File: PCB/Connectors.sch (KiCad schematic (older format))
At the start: 17 parts, among them J1 S2B-PH-SM4-TB, J10 DNP, J11 DNP, J12 DNP, J2 TRANSDUCER, J3 DNP, J4 PH1-08-UA, J5 DNP, J6 DNP, J7 DNP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

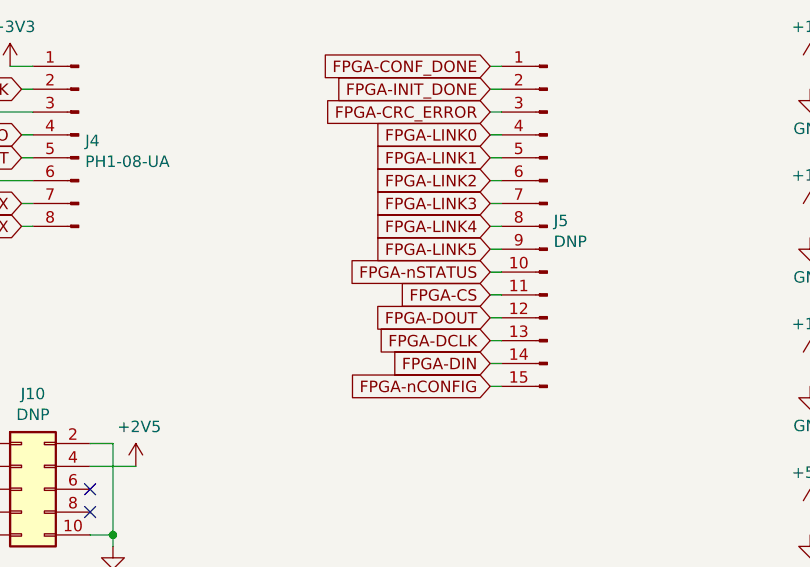
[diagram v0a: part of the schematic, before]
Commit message: Move FPGA SPI-DOUT pin to make Quartus happy
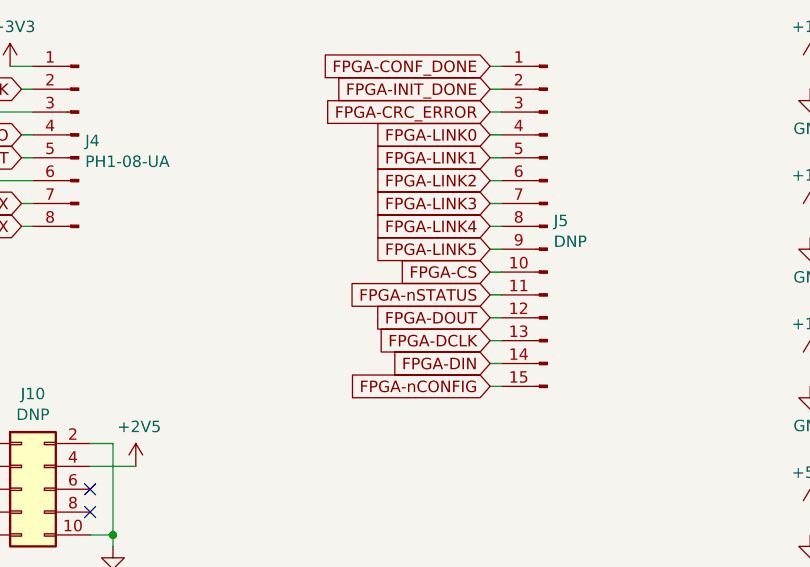
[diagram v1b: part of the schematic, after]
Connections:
- net FPGA-CS: now also J5.10 (Pin_10); no longer J5.11 (Pin_11)
- net FPGA-nSTATUS: now also J5.11 (Pin_11); no longer J5.10 (Pin_10)
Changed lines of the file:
@@
 Text GLabel 4800 5000 0    50   Input ~ 0
 FPGA-DOUT
-Text GLabel 4800 4800 0    50   Input ~ 0
+Text GLabel 4800 4900 0    50   Input ~ 0
 FPGA-nSTATUS
 Text GLabel 4800 5100 0    50   Input ~ 0
@@
 Wire Wire Line
 	6300 4550 6200 4550
-Text GLabel 4800 4900 0    50   Input ~ 0
+Text GLabel 4800 4800 0    50   Input ~ 0
 FPGA-CS
 Text GLabel 8800 4600 0    50   Input ~ 0

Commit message: Tiny fixes to the schematic
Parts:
- J8: value PH1-08-UA -> DNP
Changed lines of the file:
@@
 P 9050 5200
 F 0 "J8" H 9022 5174 50  0000 R CNN
-F 1 "PH1-08-UA" H 9022 5083 50  0000 R CNN
+F 1 "DNP" H 9022 5083 50  0000 R CNN
 F 2 "Pin_Headers:Pin_Header_Straight_1x08_Pitch2.54mm" H 9050 5200 50  0001 C CNN
 F 3 "https://www.digikey.ca/product-detail/en/adam-tech/PH1-08-UA/2057-PH1-08-UA-ND/9830442" H 9050 5200 50  0001 C CNN
